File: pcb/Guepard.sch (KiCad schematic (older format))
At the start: 3 parts, among them J2 DB25, J3 DB9, J4 DB9

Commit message: update
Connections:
- net Injector-GND: now also J2.24 (P24)
- net RPM-Crank-IN-GND: now reaches J2.6
- net MAT-Sensor renamed SPR-Sensor
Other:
- note removed: "5vdc-cpu = VDD\n\n5vdc-analog = VCC\n\nINJ-GND and INJ-GND2 are isolated to only be used by the Injector FETs"
- note removed: "J2 is the TE Connectivity Automotive Grade water resistant connector. \nThe 35 positions will allow for modifications to the board for additional \ninputs/outputs as this design only uses 27 positions. My samples to\ntest have arrived, http://www.te.com Part #'s:\n\n1-776163-2 Right Angle 35 Position Header (Natural Color)\nOR\n1-776231-2 Vertical 35 Position Header (Natural Color)\n1-776231-2 Ve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"
- note removed: "Jumpers labeled JP5 and JP6 are crossover wires,nothing \nmore. This was done to ease single sided PCB Prototype testing."
- note removed: "Make sure that the PCB grounds do not touch the inside of the case and \nisolate the TO-220 voltage regulators from the end panels of the case\nwith mica insulators and use plastic screws."
- note removed: "Notes:"
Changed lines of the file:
@@
-EESchema Schematic File Version 2  date 23/05/2013 15:10:10
+EESchema Schematic File Version 2  date 24/05/2013 14:40:27
 LIBS:opto
 LIBS:power
@@
 Sheet 1 8
 Title "Guepard PCB for FreeEMS"
-Date "23 may 2013"
+Date "24 may 2013"
 Rev "0.1-alpha"
 Comp ""
@@
 Comment4 ""
 $EndDescr
+Text GLabel 5550 4450 0    40   Input ~ 0
+Injector-GND
+Text HLabel 9300 6550 2    40   Input ~ 0
+RPM0-IN-GND
+Text GLabel 9300 6550 0    40   Input ~ 0
+RPM-Crank-IN-GND
+Text GLabel 5550 5550 0    40   Input ~ 0
+RPM-Crank-IN-GND
+Wire Wire Line
+	5550 6350 4800 6350
+Wire Wire Line
+	4800 6150 5550 6150
+Connection ~ 5150 4850
+Wire Wire Line
+	5550 4650 5150 4650
+Wire Wire Line
+	7500 5650 7250 5650
+Wire Wire Line
+	7250 5650 7250 5700
+Connection ~ 7400 5550
+Wire Wire Line
+	7250 5550 7500 5550
+Wire Wire Line
+	9050 1500 8550 1500
+Wire Wire Line
+	8550 1500 8550 2200
+Wire Wire Line
+	8550 2200 9050 2200
+Connection ~ 8550 2200
+Connection ~ 9050 2200
+Connection ~ 9050 1500
+Wire Wire Line
+	7500 5750 7400 5750
+Wire Wire Line
+	7400 5750 7400 5550
+Connection ~ 7400 5650
+Wire Wire Line
+	5550 4850 4950 4850
+Wire Wire Line
+	4950 4850 4950 4900
+Wire Wire Line
+	5150 4650 5150 5050
+Wire Wire Line
+	5150 5050 5550 5050
+Wire Wire Line
+	7500 4900 7500 5100
+Connection ~ 7500 5000
+Wire Wire Line
+	5550 5950 4800 5950
+Wire Wire Line
+	4800 5950 4800 6350
+Connection ~ 4800 6150
 Text Notes 4650 5950 0    40   ~ 0
 Sensor Ground
-Connection ~ 4800 6150
-Wire Wire Line
-	4800 5950 4800 6350
-Wire Wire Line
-	4800 5950 5550 5950
-Connection ~ 7500 5000
-Wire Wire Line
-	7500 4900 7500 5100
-Wire Wire Line
-	5550 5050 5150 5050
-Wire Wire Line
-	5150 5050 5150 4650
-Wire Wire Line
-	4950 4900 4950 4850
-Wire Wire Line
-	4950 4850 5550 4850
-Connection ~ 7400 5650
-Wire Wire Line
-	7400 5550 7400 5750
-Wire Wire Line
-	7400 5750 7500 5750
-Connection ~ 9050 1500
-Connection ~ 9050 2200
-Connection ~ 8550 2200
-Wire Wire Line
-	9050 2200 8550 2200
-Wire Wire Line
-	8550 2200 8550 1500
-Wire Wire Line
-	8550 1500 9050 1500
-Wire Notes Line
-	550  2050 4200 2050
-Wire Notes Line
-	550  1050 4200 1050
-Wire Notes Line
-	4200 550  550  550
-Wire Notes Line
-	4200 550  4200 7750
-Wire Notes Line
-	4200 7750 550  7750
-Wire Notes Line
-	550  7750 550  550
-Wire Notes Line
-	550  2450 4200 2450
-Wire Wire Line
-	7250 5550 7500 5550
-Connection ~ 7400 5550
-Wire Wire Line
-	7250 5700 7250 5650
-Wire Wire Line
-	7250 5650 7500 5650
-Wire Wire Line
-	5150 4650 5550 4650
-Connection ~ 5150 4850
-Wire Wire Line
-	4800 6150 5550 6150
-Wire Wire Line
-	4800 6350 5550 6350
 Text GLabel 7500 5000 0    40   Input ~ 0
 Output-Ground
@@
 Output-Ground
 $Comp
-L GND #PWR01
+L GND #PWR1
 U 1 1 519E0B3D
 P 4950 4900
-F 0 "#PWR01" H 4950 4900 30  0001 C CNN
+F 0 "#PWR1" H 4950 4900 30  0001 C CNN
 F 1 "GND" H 4950 4830 30  0001 C CNN
 	1    4950 4900
@@
 +12V-ACC
 $Comp
-L GND #PWR02
+L GND #PWR2
 U 1 1 519E06BD
 P 7250 5700
-F 0 "#PWR02" H 7250 5700 30  0001 C CNN
+F 0 "#PWR2" H 7250 5700 30  0001 C CNN
 F 1 "GND" H 7250 5630 30  0001 C CNN
 	1    7250 5700
@@
 $EndSheet
 Text GLabel 5550 6550 0    40   Input ~ 0
-MAT-Sensor
+SPR-Sensor
 Text GLabel 5550 5450 0    40   Input ~ 0
 RPM-Crank-IN-
@@
 Coolant-Sensor
 Text GLabel 9300 5250 0    40   Input ~ 0
-MAT-Sensor
+SPR-Sensor
 Text GLabel 9300 5150 0    40   Input ~ 0
 IAT-Sensor
@@
 Text HLabel 10650 2800 0    40   Input ~ 0
 Spare-LSD-3
-Text HLabel 6900 2350 0    40   Input ~ 0
+Text HLabel 3200 2550 0    40   Input ~ 0
 PA7
-Text GLabel 6900 2350 2    40   Output ~ 0
+Text GLabel 3200 2550 2    40   Output ~ 0
 Fuel-Pump-Drive
 Text GLabel 9050 2700 0    40   Input ~ 0
@@
 Text GLabel 9200 3850 0    40   Input ~ 0
 5vdc-analog
-Text GLabel 6900 750  2    40   Output ~ 0
+Text GLabel 3200 950  2    40   Output ~ 0
 CPU-PT2
-Text GLabel 6900 850  2    40   Output ~ 0
+Text GLabel 3200 1050 2    40   Output ~ 0
 CPU-PT3
-Text HLabel 6900 1250 0    40   Input ~ 0
+Text HLabel 3200 1450 0    40   Input ~ 0
 PT7
-Text HLabel 6900 1150 0    40   Input ~ 0
+Text HLabel 3200 1350 0    40   Input ~ 0
 PT6
 Text GLabel 10650 5050 2    40   Output ~ 0
 AAP
-Text GLabel 5200 2200 0    40   Input ~ 0
+Text GLabel 1500 2400 0    40   Input ~ 0
 AAP
 Text GLabel 9050 2300 0    40   Input ~ 0
@@
 Text GLabel 5450 3200 0    40   Input ~ 0
 Ground
-Text GLabel 5200 2400 0    40   Input ~ 0
+Text GLabel 1500 2600 0    40   Input ~ 0
 Ground
 Text GLabel 10600 1550 2    40   Input ~ 0
@@
 Text Notes 4950 2950 0    40   ~ 0
 12v-Constant
-Text Notes 650  2600 0    60   ~ 0
-5vdc-cpu = VDD\n\n5vdc-analog = VCC\n\nINJ-GND and INJ-GND2 are isolated to only be used by the Injector FETs
-Text Notes 650  2200 0    60   ~ 0
-Make sure that the PCB grounds do not touch the inside of the case and \nisolate the TO-220 voltage regulators from the end panels of the case\nwith mica insulators and use plastic screws.
-Text GLabel 6900 1250 2    40   Output ~ 0
+Text GLabel 3200 1450 2    40   Output ~ 0
 CPU-PT7
-Text GLabel 6900 1150 2    40   Output ~ 0
+Text GLabel 3200 1350 2    40   Output ~ 0
 CPU-PT6
-Text GLabel 6900 1050 2    40   Output ~ 0
+Text GLabel 3200 1250 2    40   Output ~ 0
 CPU-PT5
-Text GLabel 6900 950  2    40   Output ~ 0
+Text GLabel 3200 1150 2    40   Output ~ 0
 CPU-PT4
 Text GLabel 9050 1000 0    40   Input ~ 0
@@
 Injector1/3-IN
 $Sheet
-S 5200 700  1700 1800
+S 1500 900  1700 1800
 U 4F0A2F06
 F0 "CPU" 40
 F1 "cpu.sch" 40
-F2 "MAT-Signal" I L 5200 2100 40
-F3 "BRV-Signal" I L 5200 1800 40
-F4 "MAP-Signal" I L 5200 1700 40
-F5 "O2-Signal" I L 5200 2000 40
-F6 "TPS-Signal" I L 5200 1900 40
-F7 "Coolant-Signal" I L 5200 1600 40
-F8 "IAT-Signal" I L 5200 1500 40
-F9 "AAP-Signal" I L 5200 2200 40
-F10 "5vdc-analog" I L 5200 850 40
-F11 "5vdc-cpu" I L 5200 750 40
-F12 "PT4" O R 6900 950 40
-F13 "PT3" O R 6900 850 40
-F14 "PT2" O R 6900 750 40
-F15 "PT5" O R 6900 1050 40
-F16 "PCB-GND" I L 5200 2400 40
-F17 "RPM0" I L 5200 1250 40
-$EndSheet
-Text Notes 650  1200 0    60   ~ 0
-J2 is the TE Connectivity Automotive Grade water resistant connector. \nThe 35 positions will allow for modifications to the board for additional \ninputs/outputs as this design only uses 27 positions.  My samples to\ntest have arrived, http://www.te.com Part #'s:\n\n1-776163-2 Right Angle 35 Position Header (Natural Color)\nOR\n1-776231-2 Vertical 35 Position Header (Natural Color)\n1-776231-2 Vertical 35 Position Header (Natural Color)\n776164-2 35 Position AMP SEAL Plug Assembly (Natural Color)
-Text Notes 650  900  0    60   ~ 0
-Jumpers labeled JP5 and JP6 are crossover wires,nothing \nmore.  This was done to ease single sided PCB Prototype testing.
-Text Notes 600  700  0    70   ~ 14
-Notes:
+F2 "SPR-Signal" I L 1500 2300 40
+F3 "BRV-Signal" I L 1500 2000 40
+F4 "MAP-Signal" I L 1500 1900 40
+F5 "O2-Signal" I L 1500 2200 40
+F6 "TPS-Signal" I L 1500 2100 40
+F7 "Coolant-Signal" I L 1500 1800 40
+F8 "IAT-Signal" I L 1500 1700 40
+F9 "AAP-Signal" I L 1500 2400 40
+F10 "5vdc-analog" I L 1500 1050 40
+F11 "5vdc-cpu" I L 1500 950 40
+F12 "PT4" O R 3200 1150 40
+F13 "PT3" O R 3200 1050 40
+F14 "PT2" O R 3200 950 40
+F15 "PT5" O R 3200 1250 40
+F16 "PCB-GND" I L 1500 2600 40
+F17 "RPM0" I L 1500 1450 40
+$EndSheet
 $Sheet
 S 9300 4850 1350 1900
@@
 F10 "TPS-CPU-Signal" O R 10650 5350 40
 F11 "TPS-Sensor" I L 9300 5550 40
-F12 "MAT-Sensor" I L 9300 5250 40
-F13 "MAT-CPU-Signal" O R 10650 5650 40
+F12 "SPR-Sensor" I L 9300 5250 40
+F13 "SPR-CPU-Signal" O R 10650 5650 40
 F14 "BRV" O R 10650 4900 40
 F15 "MAP-CPU-Signal" O R 10650 5150 40
@@
 Text GLabel 9300 5000 0    40   Input ~ 0
 5vdc-analog
-Text GLabel 5200 850  0    40   Input ~ 0
+Text GLabel 1500 1050 0    40   Input ~ 0
 5vdc-analog
-Text GLabel 5200 1800 0    40   Input ~ 0
+Text GLabel 1500 2000 0    40   Input ~ 0
 BRV
 Text GLabel 9050 2800 0    40   Input ~ 0
@@
 Text GLabel 10650 6550 2    40   Output ~ 0
 RPM0
-Text GLabel 5200 2000 0    40   Input ~ 0
+Text GLabel 1500 2200 0    40   Input ~ 0
 O2
 Text GLabel 10650 5550 2    40   Output ~ 0
 O2
-Text GLabel 5200 1900 0    40   Input ~ 0
+Text GLabel 1500 2100 0    40   Input ~ 0
 TPS
 Text GLabel 10650 5350 2    40   Output ~ 0
 TPS
-Text GLabel 5200 1600 0    40   Input ~ 0
+Text GLabel 1500 1800 0    40   Input ~ 0
 COOLANT
 Text GLabel 10650 5450 2    40   Output ~ 0
 COOLANT
-Text GLabel 5200 2100 0    40   Input ~ 0
-MAT
+Text GLabel 1500 2300 0    40   Input ~ 0
+SPR
 Text GLabel 10650 5650 2    40   Output ~ 0
-MAT
-Text GLabel 5200 1500 0    40   Input ~ 0
+SPR
+Text GLabel 1500 1700 0    40   Input ~ 0
 IAT
 Text GLabel 10650 5250 2    40   Output ~ 0
@@
 Text GLabel 10650 4900 2    40   Output ~ 0
 BRV
-Text GLabel 5200 1250 0    40   Input ~ 0
+Text GLabel 1500 1450 0    40   Input ~ 0
 RPM0
-Text GLabel 5200 1700 0    40   Input ~ 0
+Text GLabel 1500 1900 0    40   Input ~ 0
 MAP
-Text GLabel 5200 750  0    40   Input ~ 0
+Text GLabel 1500 950  0    40   Input ~ 0
 5vdc-cpu
 Text GLabel 6500 3000 2    40   Output ~ 0

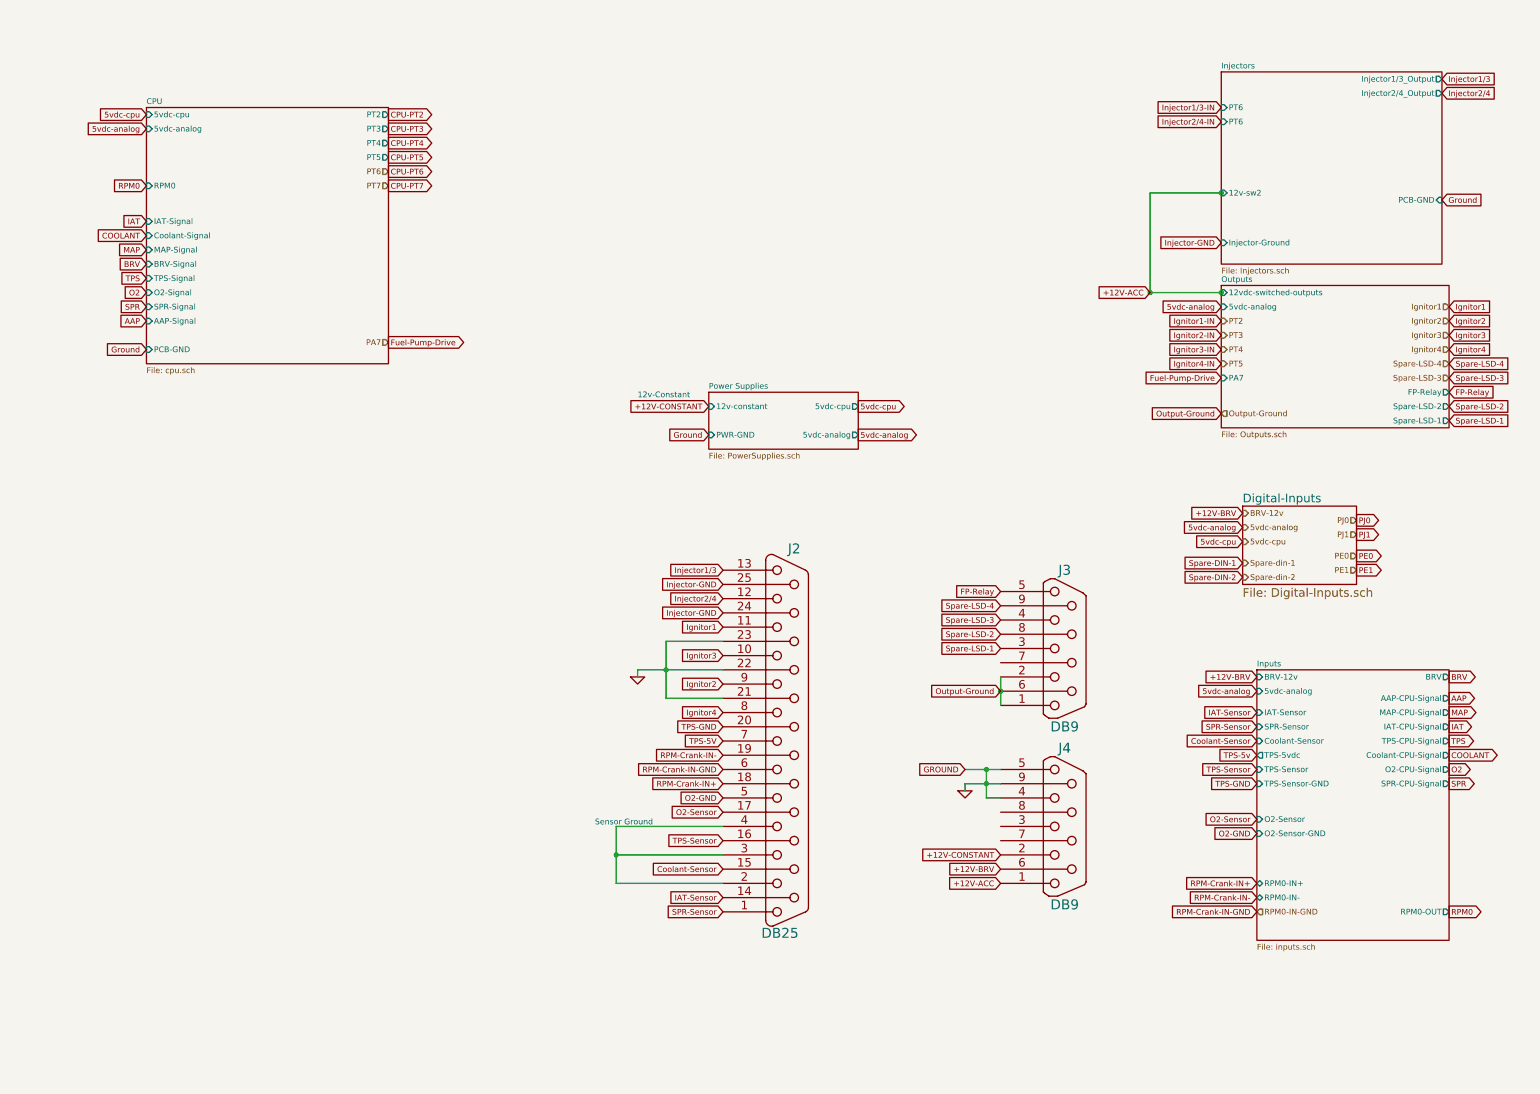
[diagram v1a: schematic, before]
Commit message: schematics update
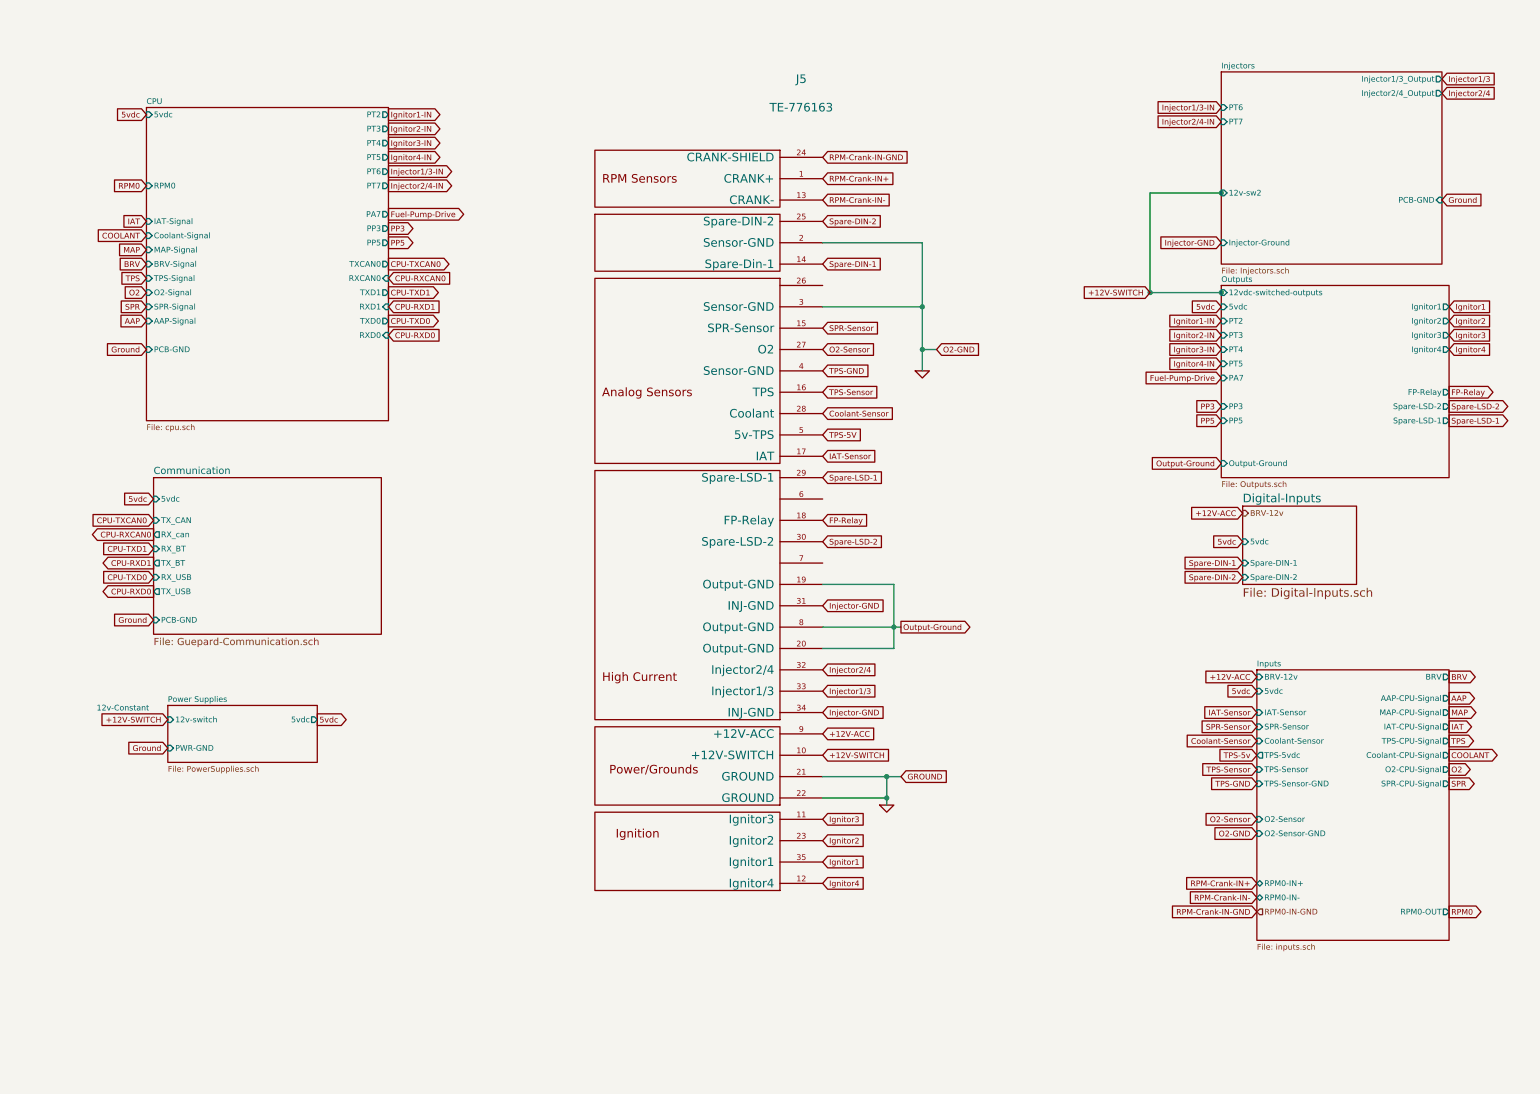
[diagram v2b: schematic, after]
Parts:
- removed J2: DB25, symbol DB25
- removed J3, J4: DB9, symbol DB9
- added J5: TE-776163, ~, symbol TE-776163
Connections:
- net +12V-ACC: now also J5.9 (+12V-ACC)
- net Coolant-Sensor: now also J5.28 (Coolant)
- net FP-Relay: now also J5.18 (FP-Relay)
- net GND: now also J5.2 (Sensor-GND), J5.21 (GROUND), J5.22 (GROUND), J5.3 (Sensor-GND)
- net IAT-Sensor: now also J5.17 (IAT)
- net Ignitor1: now also J5.35 (Ignitor1)
- net Ignitor2: now also J5.23 (Ignitor2)
- net Ignitor3: now also J5.11 (Ignitor3)
- net Ignitor4: now also J5.12 (Ignitor4)
- net Injector-GND: now also J5.31 (INJ-GND), J5.34 (INJ-GND)
- net Injector1/3: now also J5.33 (Injector1/3)
- net Injector2/4: now also J5.32 (Injector2/4)
- net O2-Sensor: now also J5.27 (O2)
- net Output-Ground: now also J5.19 (Output-GND), J5.20 (Output-GND), J5.8 (Output-GND)
- net RPM-Crank-IN+: now also J5.1 (CRANK+)
- net RPM-Crank-IN-: now also J5.13 (CRANK-)
- net RPM-Crank-IN-GND: now also J5.24 (CRANK-SHIELD)
- net SPR-Sensor: now also J5.15 (SPR-Sensor)
- net Spare-DIN-1: now also J5.14 (Spare-Din-1)
- net Spare-DIN-2: now also J5.25 (Spare-DIN-2)
- net Spare-LSD-1: now also J5.29 (Spare-LSD-1)
- net Spare-LSD-2: now also J5.30 (Spare-LSD-2)
- net TPS-5V: now also J5.5 (5v-TPS)
- net TPS-GND: now also J5.4 (Sensor-GND)
- net TPS-Sensor: now also J5.16 (TPS)
- new net +12V-SWITCH: J5.10 (+12V-SWITCH)
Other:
- note removed: "Sensor Ground"
